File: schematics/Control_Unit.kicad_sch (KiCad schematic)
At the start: 75 parts, among them SW1 SW_Push, U1 28C256, U2 28C256, U3 74LS161, U4 28C256, U5 74LS00, U6 74LS04, U7 74LS04, U8 74LS04, U9 74LS04

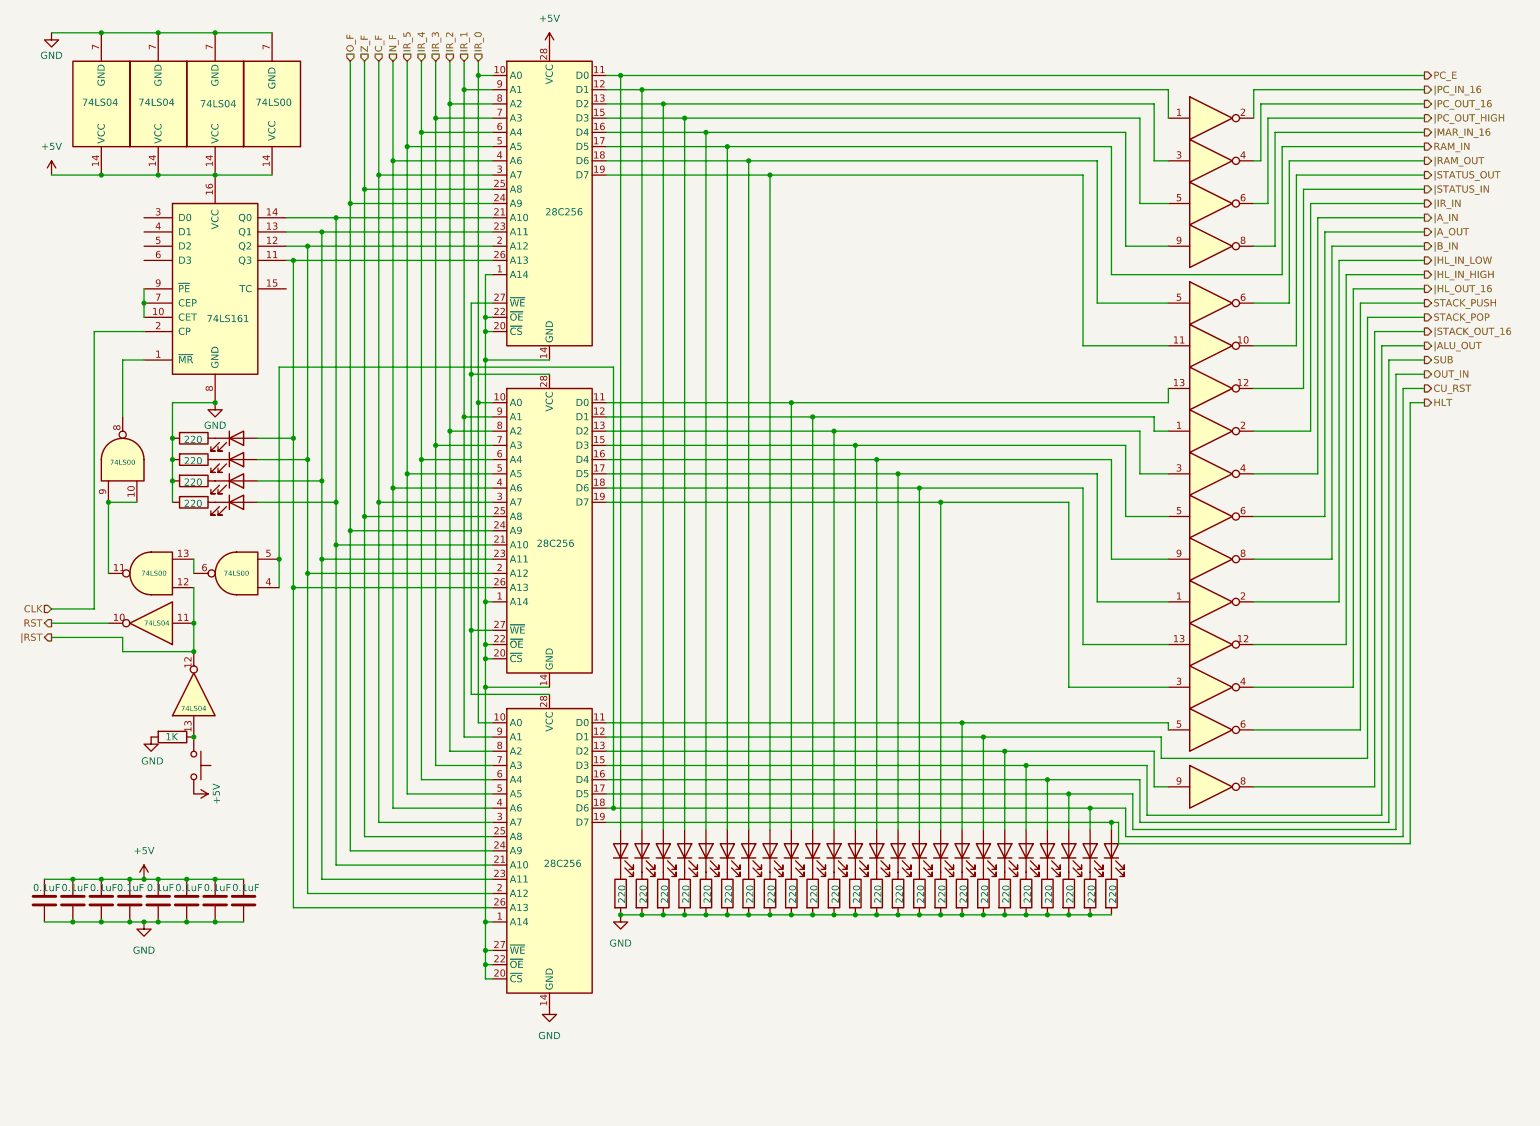
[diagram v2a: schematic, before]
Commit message: Updated schematics and README
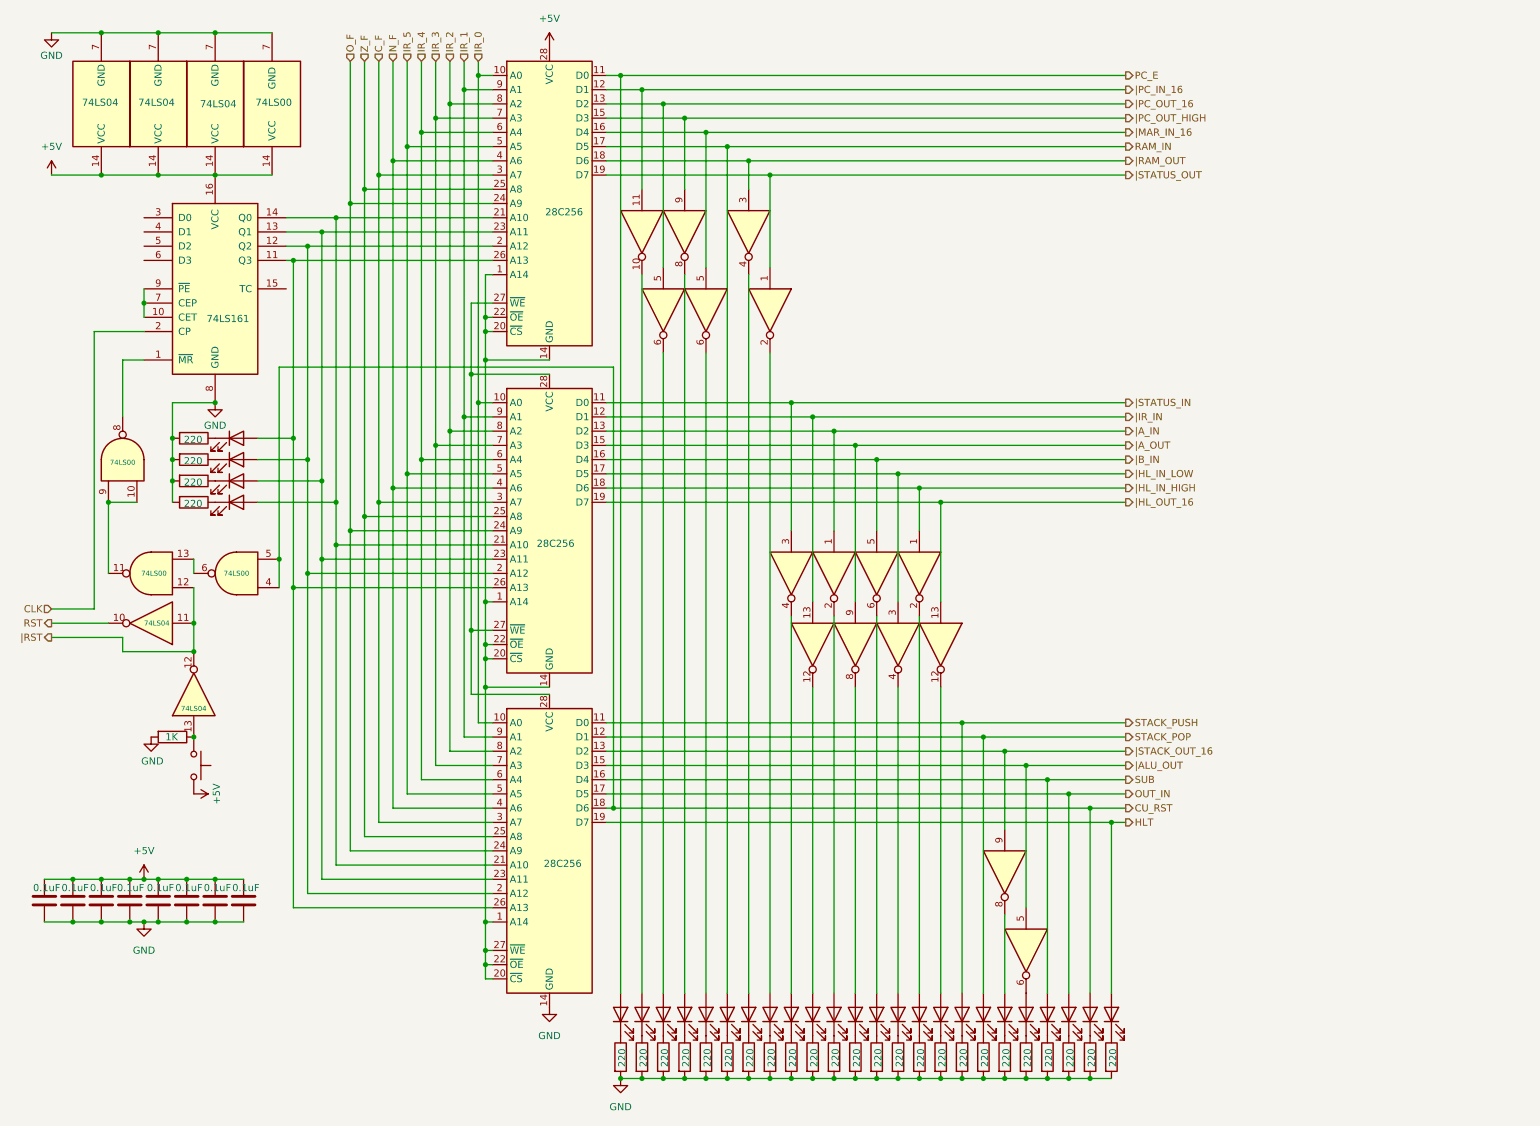
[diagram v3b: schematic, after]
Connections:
- net STACK_PUSH: now also D18.2 (A), U4.11 (D0); no longer U8.6
- net |ALU_OUT: now also U8.5; no longer D21.2 (A)
- net |A_IN: now also U2.13 (D2), U8.1; no longer U7.4
- net |A_OUT: now also U2.15 (D3), U7.9; no longer U7.6
- net |B_IN: now also U2.16 (D4), U7.5; no longer U7.8
- net |HL_IN_HIGH: now also U2.18 (D6), U7.1; no longer U8.12
- net |HL_IN_LOW: now also U2.17 (D5), U7.3; no longer U8.2
- net |HL_OUT_16: now also U2.19 (D7), U6.13; no longer U8.4
- net |IR_IN: now also U2.12 (D1), U8.13; no longer U7.2
- net |MAR_IN_16: now also U1.16 (D4), U6.5; no longer U6.8
- net |PC_IN_16: now also U1.12 (D1), U6.11; no longer U6.2
- net |PC_OUT_16: now also U1.13 (D2), U9.5; no longer U6.4
- net |PC_OUT_HIGH: now also U1.15 (D3), U6.9; no longer U6.6
- net |RAM_OUT: now also U1.18 (D6), U6.3; no longer U9.6
- net |STACK_OUT_16: now also U4.13 (D2), U8.9; no longer U8.8
- net |STATUS_IN: now also U2.11 (D0), U8.3; no longer U6.12
- net |STATUS_OUT: now also U1.19 (D7), U6.1; no longer U6.10
- new net: D10.2 (A), U8.12
- new net: D4.2 (A), U6.8
- new net: D11.2 (A), U8.2
- new net: D9.2 (A), U8.4
- new net: D2.2 (A), U6.10
- new net: D8.2 (A), U6.2
- new net: D13.2 (A), U7.6
- new net: D5.2 (A), U6.6
- new net: D3.2 (A), U9.6
- new net: D20.2 (A), U8.8
- new net: D12.2 (A), U7.8
- new net: D14.2 (A), U7.4
- new net: D15.2 (A), U7.2
- new net: D16.2 (A), U6.12
- new net: D21.2 (A), U8.6
- new net: D7.2 (A), U6.4

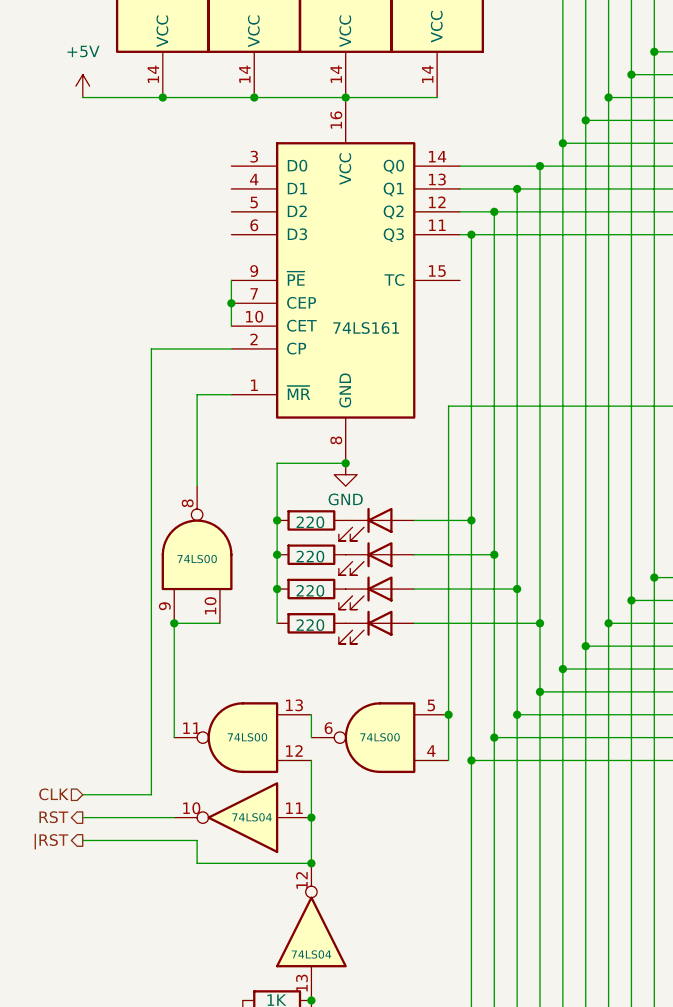
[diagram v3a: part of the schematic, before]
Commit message: Fixed Control Unit schematics (CU_RST signal synchronicity)
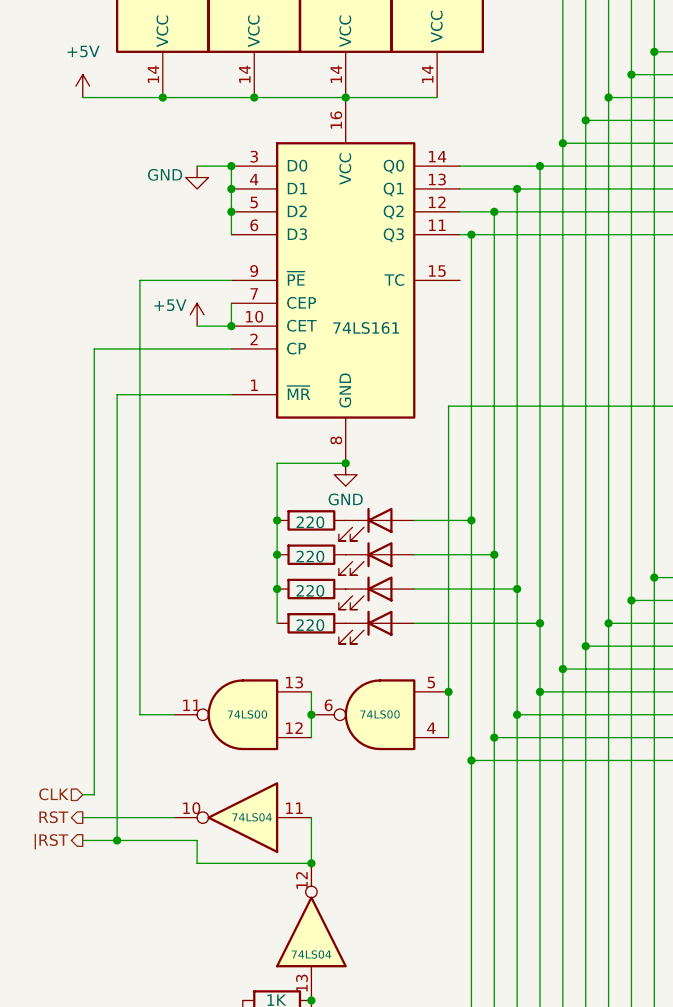
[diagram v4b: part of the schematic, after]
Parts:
- removed unit 3 of U5
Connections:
- net +5V: now also U3.10 (CET), U3.7 (CEP)
- net GND: now also U3.3 (D0), U3.4 (D1), U3.5 (D2), U3.6 (D3)
- net |RST: now also U3.1 (~{MR}); no longer U5.12
- net at U5.11: now also U3.9 (~{PE})
- net at U5.13, U5.6: now also U5.12
